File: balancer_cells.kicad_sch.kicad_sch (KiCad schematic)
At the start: 22 parts, among them U3 BQ76952PFBR

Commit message: added todos
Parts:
- renumbered BT3 to BT1, BT1 to BT3
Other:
- note added: "todo: -add undevoltage/overvoltage FET -add precharge circuit (if batteries are too low, precharge them) -discuss prediscarge circuit -check thermistor connection -check how to enter and leave shutdown mode -discuss adding a fuse -discuss using a completely different balancer-circuit -discuss adding high current output -find viable SMD thermistor"
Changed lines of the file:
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@@
+		)
+	)
+	(text "todo:\n-add undevoltage/overvoltage FET\n-add precharge circuit\n(if batteries are too low, precharge them)\n-discuss prediscarge circuit\n-check thermistor connection\n-check how to enter and leave shutdown mode\n-discuss adding a fuse\n-discuss using a completely different balancer-circuit\n-discuss adding high current output\n-find viable SMD thermistor"
+		(exclude_from_sim no)
+		(at 54.864 61.722 0)
+		(effects
+			(font
+				(size 1.27 1.27)
+			)
+			(justify left)
 		)
 	)
@@
 		(on_board yes)
 		(dnp no)
-		(fields_autoplaced yes)
-		(property "Reference" "BT3"
-			(at 46.99 107.3784 0)
-			(effects
-				(font
-					(size 1.27 1.27)
-				)
-				(justify left)
+		(property "Reference" "BT1"
+			(at 44.704 107.696 0)
+			(effects
+				(font
+					(size 1.27 1.27)
+				)
+				(justify right)
 			)
 		)
 		(property "Value" "Battery_Cell"
-			(at 46.99 109.9184 0)
-			(effects
-				(font
-					(size 1.27 1.27)
-				)
-				(justify left)
+			(at 36.322 109.982 0)
+			(effects
+				(font
+					(size 1.27 1.27)
+				)
+				(justify right)
 			)
 		)
@@
 			(project "rapid_power_module"
 				(path "/afc8cbd3-9ea8-40a2-afae-ed6bd0fe7e6e/bfae272a-4bf5-4960-b276-b4c1a7fb3062"
-					(reference "BT3")
+					(reference "BT1")
 					(unit 1)
 				)
@@
 		(on_board yes)
 		(dnp no)
-		(fields_autoplaced yes)
-		(property "Reference" "BT1"
-			(at 46.99 81.9784 0)
-			(effects
-				(font
-					(size 1.27 1.27)
-				)
-				(justify left)
+		(property "Reference" "BT3"
+			(at 42.926 83.82 0)
+			(effects
+				(font
+					(size 1.27 1.27)
+				)
+				(justify right)
 			)
 		)
 		(property "Value" "Battery_Cell"
-			(at 46.99 84.5184 0)
-			(effects
-				(font
-					(size 1.27 1.27)
-				)
-				(justify left)
+			(at 37.592 86.106 0)
+			(effects
+				(font
+					(size 1.27 1.27)
+				)
+				(justify right)
 			)
 		)
@@
 			(project "rapid_power_module"
 				(path "/afc8cbd3-9ea8-40a2-afae-ed6bd0fe7e6e/bfae272a-4bf5-4960-b276-b4c1a7fb3062"
-					(reference "BT1")
+					(reference "BT3")
 					(unit 1)
 				)

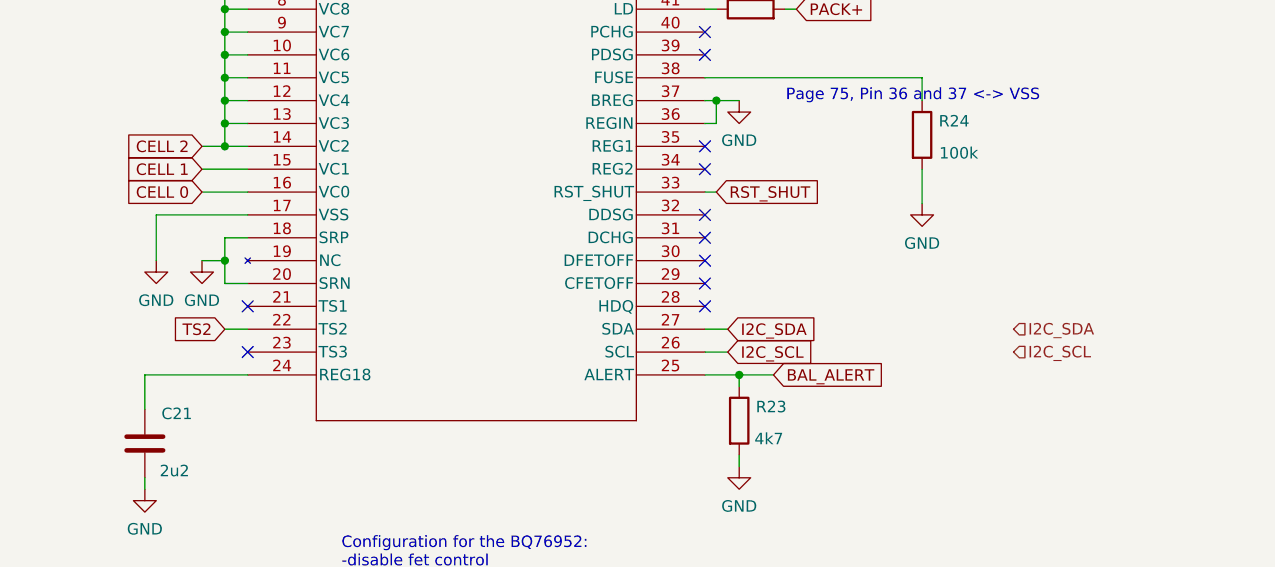
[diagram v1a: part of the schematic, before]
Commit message: added hierarchical pins for submodules
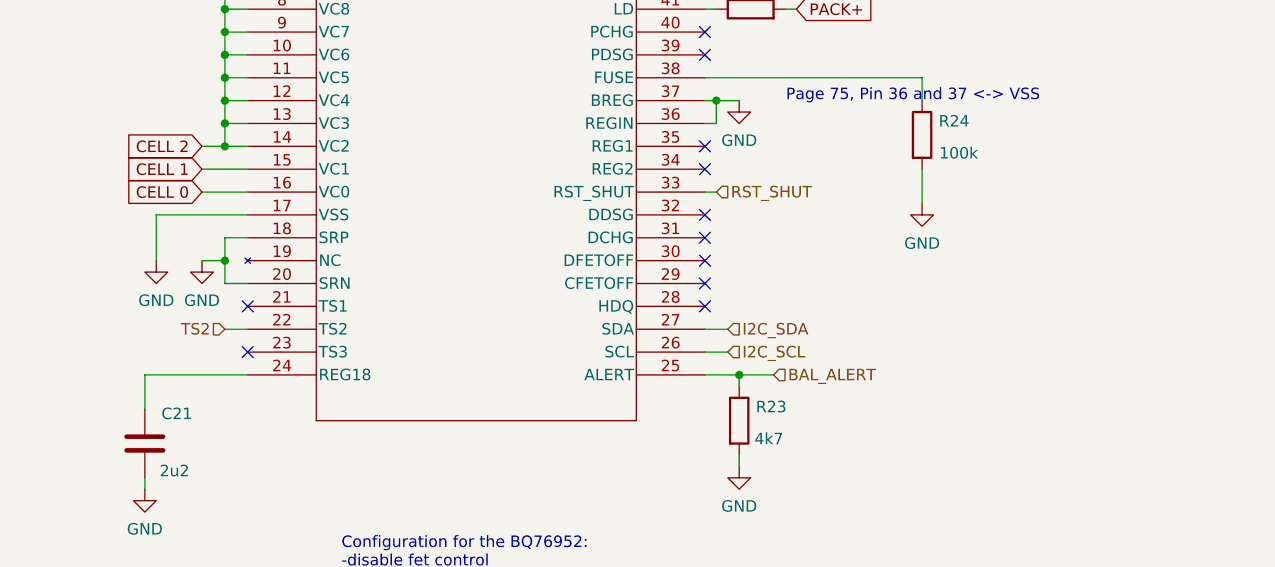
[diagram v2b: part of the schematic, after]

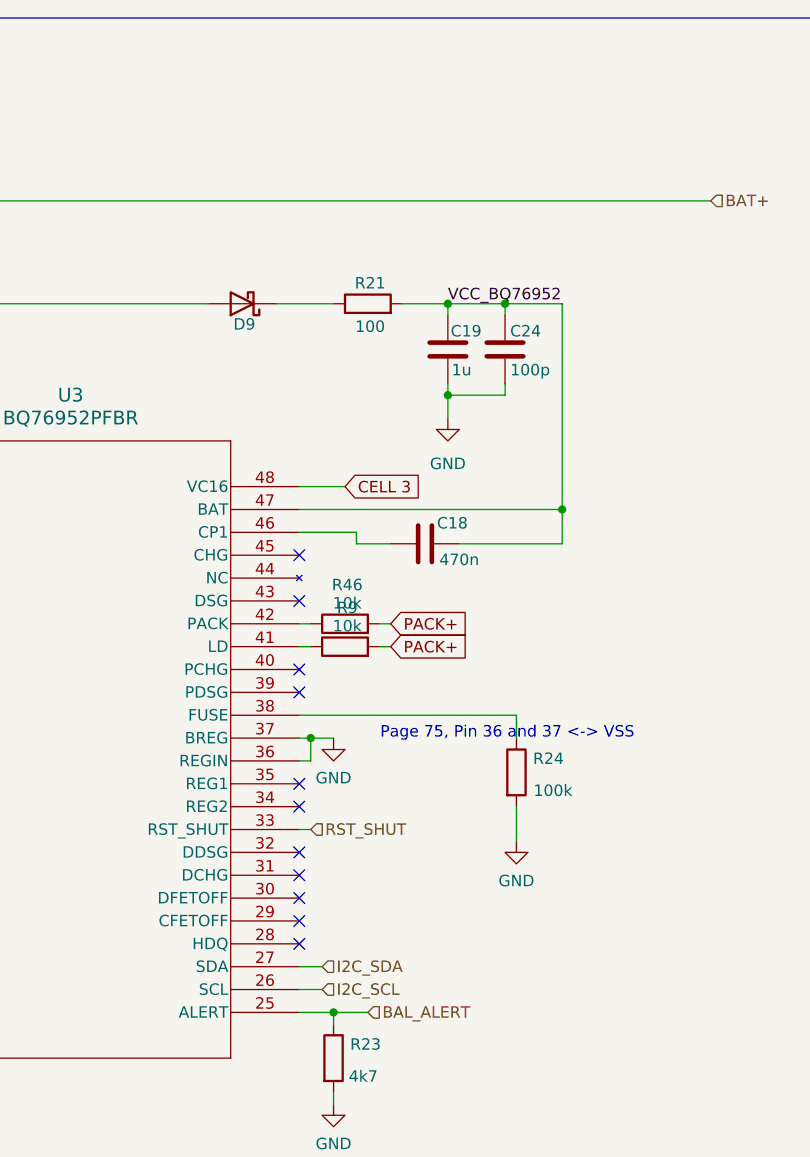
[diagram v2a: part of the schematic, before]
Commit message: added second i2c bus; cleaned up sub-schematic-structure
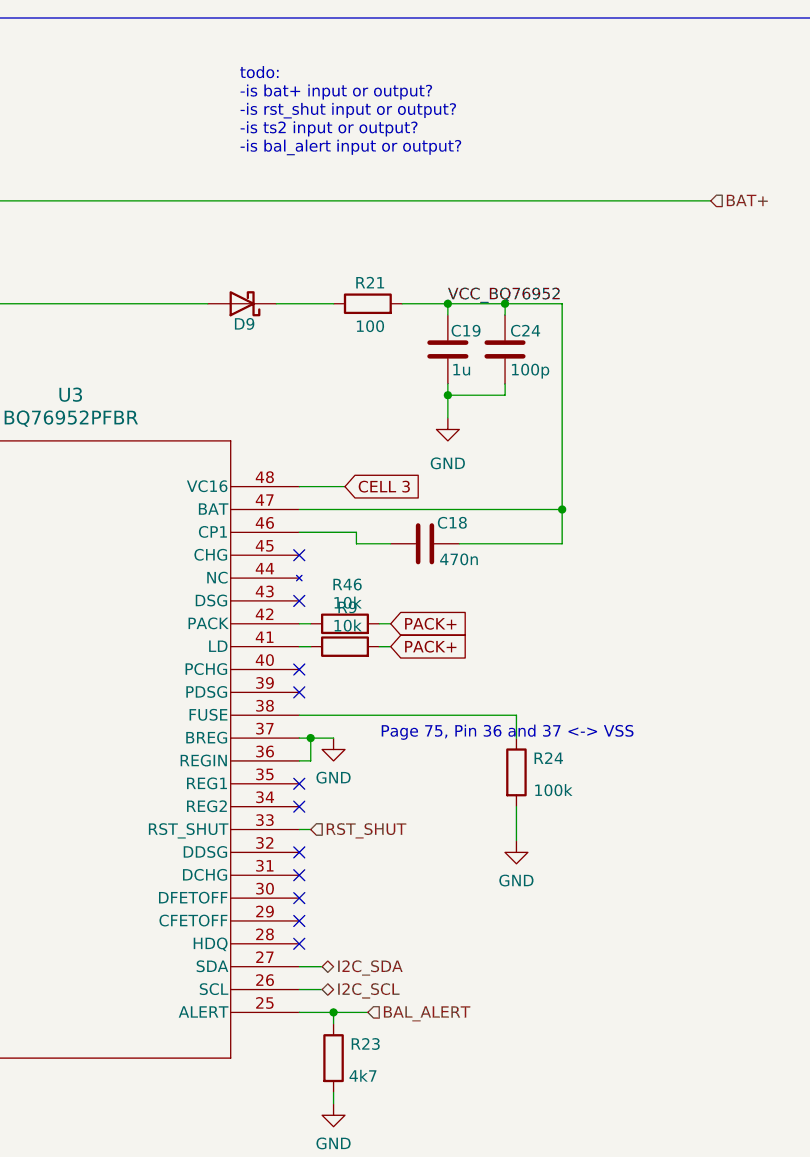
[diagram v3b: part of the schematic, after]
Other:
- note added: "todo: -is bat+ input or output? -is rst_shut input or output? -is ts2 input or output? -is bal_alert input or output?"
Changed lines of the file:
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@@
+		)
+	)
+	(text "todo:\n-is bat+ input or output?\n-is rst_shut input or output?\n-is ts2 input or output?\n-is bal_alert input or output?"
+		(exclude_from_sim no)
+		(at 162.306 28.194 0)
+		(effects
+			(font
+				(size 1.27 1.27)
+			)
+			(justify left)
 		)
 	)
@@
 	)
 	(hierarchical_label "I2C_SCL"
-		(shape input)
+		(shape bidirectional)
 		(at 171.45 125.73 0)
 		(effects
@@
 	)
 	(hierarchical_label "I2C_SDA"
-		(shape input)
+		(shape bidirectional)
 		(at 171.45 123.19 0)
 		(effects

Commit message: cleaned up hierarchical structure; changed connectors
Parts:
- added Q4: NMOS, symbol Simulation_SPICE:NMOS
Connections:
- net PACK+: now also Q4.3 (S)
- net at U3.43 (DSG): now also Q4.2 (G)
- new net BAT+: Q4.1 (D)
- no-connect marks 13 -> 12
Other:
- note added: "todo: -is ts2 input or output?"
- note removed: "todo: -is bat+ input or output? -is rst_shut input or output? -is ts2 input or output? -is bal_alert input or output?"
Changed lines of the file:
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@@
 		)
 	)
-	(text "todo:\n-is bat+ input or output?\n-is rst_shut input or output?\n-is ts2 input or output?\n-is bal_alert input or output?"
+	(text "todo:\n-is ts2 input or output?"
 		(exclude_from_sim no)
 		(at 162.306 28.194 0)
@@
 	)
 	(junction
+		(at 129.54 38.1)
+		(diameter 0)
+		(color 0 0 0 0)
+	)
+	(junction
 		(at 72.39 102.87)
 		(diameter 0)
@@
 	)
 	(no_connect
-		(at 168.91 82.55)
-	)
-	(no_connect
 		(at 118.11 120.65)
 	)
@@
 	(wire
 		(pts
+			(xy 231.14 22.86) (xy 231.14 82.55)
+		)
+		(stroke
+			(width 0)
+			(type default)
+		)
+	)
+	(wire
+		(pts
 			(xy 205.74 161.29) (xy 219.71 161.29)
 		)
@@
 	(wire
 		(pts
+			(xy 143.51 22.86) (xy 143.51 30.48)
+		)
+		(stroke
+			(width 0)
+			(type default)
+		)
+	)
+	(wire
+		(pts
 			(xy 168.91 87.63) (xy 170.18 87.63)
 		)
@@
 	(wire
 		(pts
-			(xy 50.8 38.1) (xy 214.63 38.1)
+			(xy 50.8 38.1) (xy 129.54 38.1)
+		)
+		(stroke
+			(width 0)
+			(type default)
+		)
+	)
+	(wire
+		(pts
+			(xy 143.51 22.86) (xy 231.14 22.86)
 		)
 		(stroke
@@
 	(wire
 		(pts
+			(xy 168.91 82.55) (xy 231.14 82.55)
+		)
+		(stroke
+			(width 0)
+			(type default)
+		)
+	)
+	(wire
+		(pts
 			(xy 191.77 49.53) (xy 191.77 50.8)
 		)
@@
 	(wire
 		(pts
+			(xy 148.59 38.1) (xy 214.63 38.1)
+		)
+		(stroke
+			(width 0)
+			(type default)
+		)
+	)
+	(wire
+		(pts
 			(xy 185.42 58.42) (xy 185.42 59.69)
 		)
@@
 	(wire
 		(pts
+			(xy 129.54 38.1) (xy 138.43 38.1)
+		)
+		(stroke
+			(width 0)
+			(type default)
+		)
+	)
+	(wire
+		(pts
 			(xy 177.8 87.63) (xy 179.07 87.63)
 		)
@@
 		(pts
 			(xy 76.2 128.27) (xy 72.39 128.27)
+		)
+		(stroke
+			(width 0)
+			(type default)
+		)
+	)
+	(wire
+		(pts
+			(xy 129.54 34.29) (xy 129.54 38.1)
 		)
 		(stroke
@@
 		)
 	)
+	(hierarchical_label "BAT_UNSAFE+"
+		(shape output)
+		(at 129.54 34.29 90)
+		(effects
+			(font
+				(size 1.27 1.27)
+			)
+			(justify left)
+		)
+	)
 	(hierarchical_label "I2C_SCL"
 		(shape bidirectional)
@@
 	)
 	(hierarchical_label "BAL_ALERT"
-		(shape input)
+		(shape output)
 		(at 176.53 128.27 0)
 		(effects
@@
 	)
 	(hierarchical_label "BAT+"
-		(shape input)
+		(shape output)
 		(at 214.63 38.1 0)
 		(effects
@@
 					(unit 1)
 				)
+			)
+		)
+	)
+	(symbol
+		(lib_id "Simulation_SPICE:NMOS")
+		(at 143.51 35.56 270)
+		(unit 1)
+		(exclude_from_sim no)
+		(in_bom yes)
+		(on_board yes)
+		(dnp no)
+		(fields_autoplaced yes)
+		(property "Reference" "Q4"
+			(at 143.51 41.91 90)
+			(effects
+				(font
+					(size 1.27 1.27)
+				)
+			)
+		)
+		(property "Value" "NMOS"
+			(at 143.51 44.45 90)
+			(effects
+				(font
+					(size 1.27 1.27)
+				)
+			)
+		)
+		(property "Footprint" ""
+			(at 146.05 40.64 0)
+			(effects
+				(font
+					(size 1.27 1.27)
+				)
+				(hide yes)
+			)
+		)
+		(property "Datasheet" "https://ngspice.sourceforge.io/docs/ngspice-html-manual/manual.xhtml#cha_MOSFETs"
+			(at 130.81 35.56 0)
+			(effects
+				(font
+					(size 1.27 1.27)
+				)
+				(hide yes)
+			)
+		)
+		(property "Description" "N-MOSFET transistor, drain/source/gate"
+			(at 143.51 35.56 0)
+			(effects
+				(font
+					(size 1.27 1.27)
+				)
+				(hide yes)
+			)
+		)
+		(property "Sim.Device" "NMOS"
+			(at 126.365 35.56 0)
+			(effects
+				(font
+					(size 1.27 1.27)
+				)
+				(hide yes)
+			)
+		)
+		(property "Sim.Type" "VDMOS"
+			(at 124.46 35.56 0)
+			(effects
+				(font
+					(size 1.27 1.27)
+				)
+				(hide yes)
+			)
+		)
+		(property "Sim.Pins" "1=D 2=G 3=S"
+			(at 128.27 35.56 0)
+			(effects
+				(font
+					(size 1.27 1.27)
+				)
+				(hide yes)
+			)
+		)
+		(pin "1"
+		)
+		(pin "3"
+		)
+		(pin "2"
+		)
+		(instances
+			(project ""
+				(path "/afc8cbd3-9ea8-40a2-afae-ed6bd0fe7e6e/bfae272a-4bf5-4960-b276-b4c1a7fb3062"
+					(reference "Q4")
+					(unit 1)
+				)
